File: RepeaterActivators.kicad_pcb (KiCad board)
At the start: 4 copper layers, 60 parts, among them J1 AudioJack1_Grounded, J2 AudioJack2_Grounded, J3 Conn_01x06_Female, J4 8PRJ45_LED_Shielded_Radio1, J5 8PRJ45_LED_Shielded_Radio2, J6 Conn_01x02_Female, J7 Conn_01x02_Female, J8 Conn_01x02_Female, Q1 2N7000, Q2 2N7000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

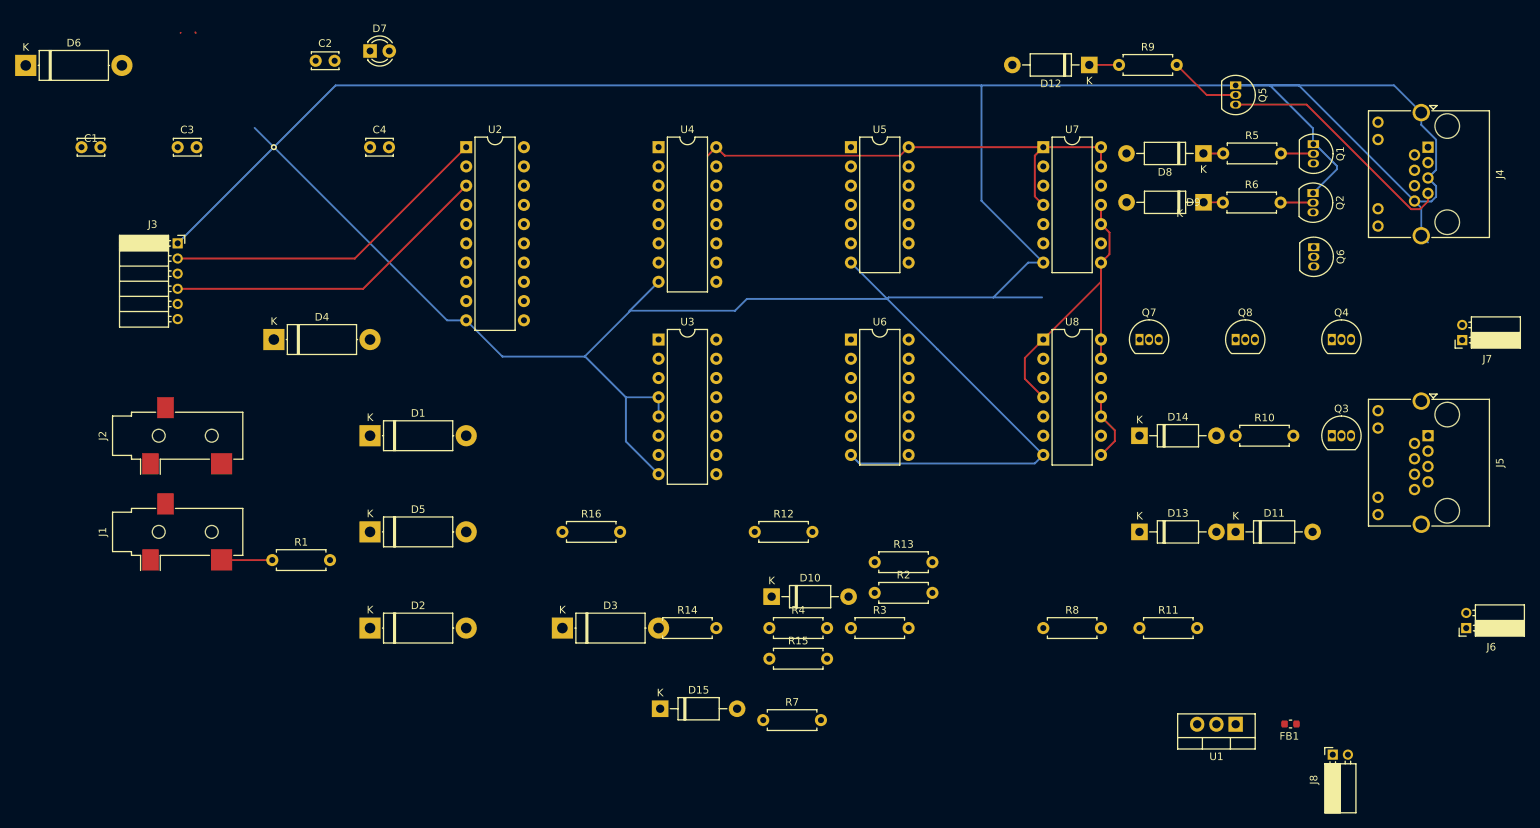
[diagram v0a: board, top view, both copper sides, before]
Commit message: DBD: positioning components on the board
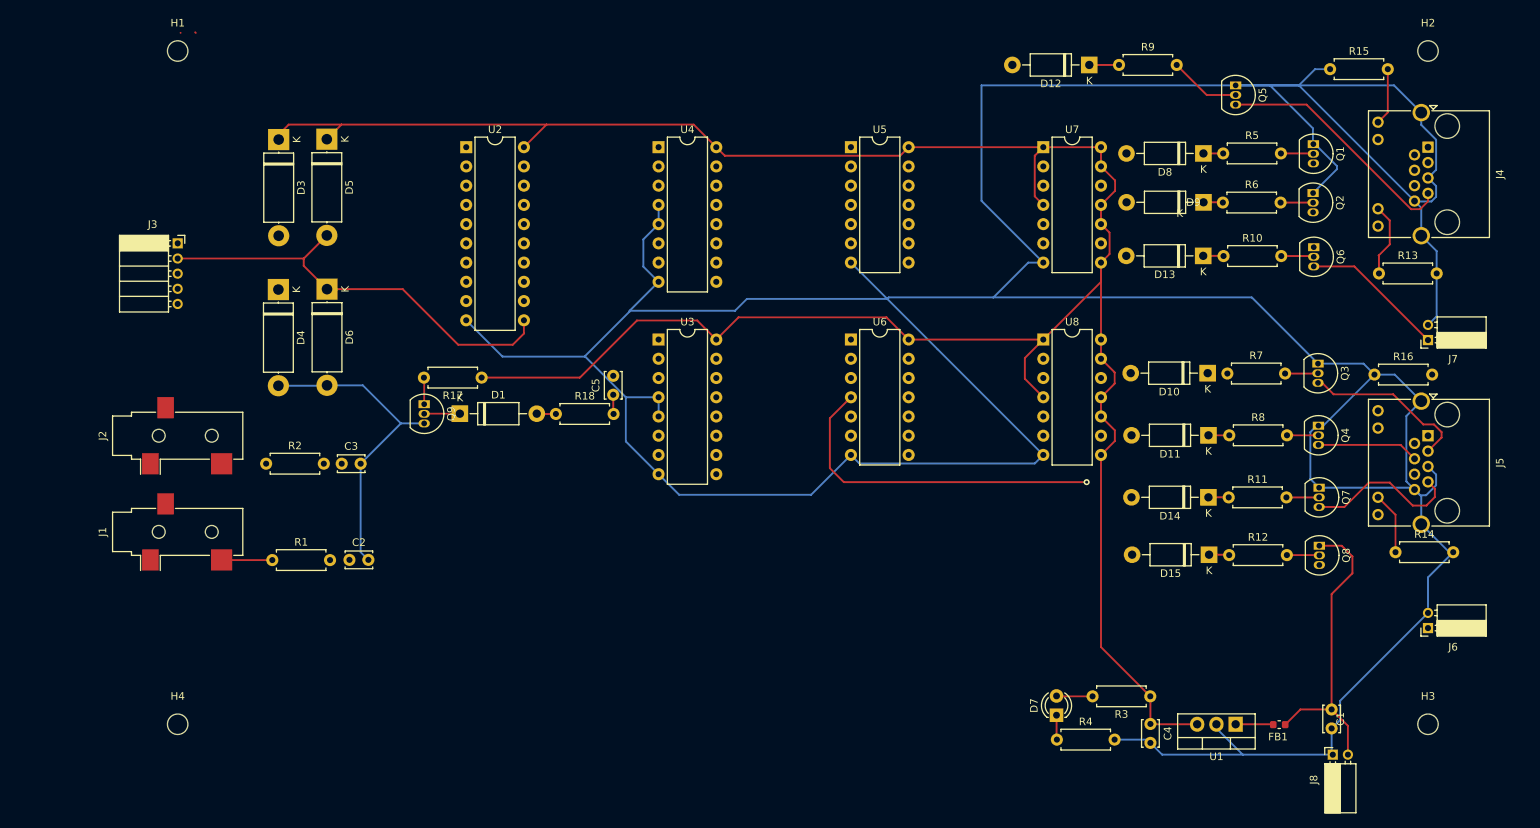
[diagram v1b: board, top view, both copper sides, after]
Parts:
- removed D2: D_Schottky, Diode_THT:D_5W_P12.70mm_Horizontal
- added C5: 100m, Capacitor_THT:C_Disc_D3.4mm_W2.1mm_P2.50mm, F.Cu at (133.7, 70.8)
- added H1: MountingHole, MountingHole:MountingHole_2.7mm_M2.5, F.Cu at (76.2, 25.4)
- added H2: MountingHole, MountingHole:MountingHole_2.7mm_M2.5, F.Cu at (241.3, 25.4)
- added H3: MountingHole, MountingHole:MountingHole_2.7mm_M2.5, F.Cu at (241.3, 114.3)
- added H4: MountingHole, MountingHole:MountingHole_2.7mm_M2.5, F.Cu at (76.2, 114.3)
- added Q9: 2N7000, Package_TO_SOT_THT:TO-92_Inline, F.Cu at (108.7, 72.0)
- added R17: 500, Resistor_THT:R_Axial_DIN0207_L6.3mm_D2.5mm_P7.62mm_Horizontal, F.Cu at (116.3, 68.5)
- added R18: 500, Resistor_THT:R_Axial_DIN0207_L6.3mm_D2.5mm_P7.62mm_Horizontal, F.Cu at (126.1, 73.3)
- D1: value D_Schottky -> 1N4001; footprint Diode_THT:D_5W_P12.70mm_Horizontal -> Diode_THT:D_DO-41_SOD81_P10.16mm_Horizontal
- J3: value Conn_01x06_Female -> Conn_01x05_Female; footprint Connector_PinSocket_2.00mm:PinSocket_1x06_P2.00mm_Horizontal -> Connector_PinSocket_2.00mm:PinSocket_1x05_P2.00mm_Horizontal
- moved C1 181.0 mm to (228.6, 112.3), turned to -90 degrees
- moved C4 128.1 mm to (204.6, 114.3), turned to -90 degrees
- moved D7 126.1 mm to (192.2, 113.1), turned to 90 degrees
- moved R16 109.2 mm to (234.2, 68.1)
- moved R15 107.4 mm to (228.4, 27.8)
- moved R14 97.8 mm to (237.0, 91.6)
- moved R2 82.2 mm to (87.9, 79.9)
- moved R13 76.7 mm to (234.8, 54.8)
- moved R7 76.5 mm to (214.8, 68.0)
- moved D15 75.3 mm to (212.4, 91.9), turned to 180 degrees
- moved D3 74.6 mm to (89.5, 37.1), turned to -90 degrees
- moved C2 66.1 mm to (98.9, 92.6)
- moved D10 64.7 mm to (212.2, 67.9), turned to 180 degrees
- moved R12 62.7 mm to (215.0, 92.0)
- moved D5 52.2 mm to (95.9, 37.0), turned to -90 degrees
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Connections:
- D1 pad 1: /|CLR -> Net-(D1-Pad1)
- D1 pad 2: GND -> Net-(D1-Pad2)
- J3 pad 2: /|CLR -> /Clock Pulse
- J3 pad 3: /Clock Pulse -> /Data Input
- J3 pad 4: /Data Input -> SPI_RPi_Radio2
- J3 pad 5: SPI_RPi_Radio2 -> SPI_RPi_Radio1
- U2 pad 1: /|CLR -> Net-(U2-Pad1)
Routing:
- net +5V: track 117.8 -> 321.7 mm
- net GND: track 495.0 -> 627.9 mm, vias 1 -> 0
- net +12V: track 0.02 -> 87.6 mm
- net Net-(D11-Pad2): track 0.00 -> 55.4 mm, vias 0 -> 1
- net Net-(D10-Pad2): track 0.00 -> 52.0 mm
- net /|CLR: track 44.2 -> 0.00 mm
- net Net-(U2-Pad1): track 0.00 -> 36.3 mm
- net Net-(D14-Pad2): track 0.00 -> 32.9 mm
- net Net-(D15-Pad2): track 0.00 -> 23.8 mm
- net /Radio2 Frequency Down: track 0.00 -> 22.3 mm
- net Net-(J5-Pad7): track 0.00 -> 20.7 mm
- net /Radio1 Fan: track 0.55 -> 19.1 mm
- net /Radio2 Fan: track 0.00 -> 17.8 mm
- net /Radio2 Frequency Up: track 0.00 -> 13.4 mm
- net Net-(J4-Pad11): track 0.00 -> 9.81 mm
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
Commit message: DBD: Routing complete sans minor errors
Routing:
- net SPI_RPi_Radio1: track 0.00 -> 228.5 mm, vias 0 -> 1
- net Audio_RPi_Radio1: track 0.00 -> 211.8 mm
- net SPI_RPi_Radio2: track 0.00 -> 195.4 mm, vias 0 -> 1
- net Audio_RPi_Radio2: track 0.00 -> 159.4 mm, vias 0 -> 2
- net Net-(U3-Pad10): track 0.00 -> 93.4 mm, vias 0 -> 3
- net Net-(U3-Pad11): track 0.00 -> 77.4 mm, vias 0 -> 3
- net GND: track 627.9 -> 700.2 mm
- net Net-(D8-Pad2): track 0.09 -> 71.2 mm
- net Net-(U3-Pad12): track 0.00 -> 67.9 mm, vias 0 -> 1
- net Net-(U4-Pad14): track 0.00 -> 66.4 mm, vias 0 -> 2
- net Net-(U2-Pad2): track 0.00 -> 56.1 mm
- net Net-(U5-Pad2): track 0.00 -> 52.5 mm
- net Net-(U4-Pad6): track 0.00 -> 52.3 mm
- net Net-(U2-Pad13): track 0.00 -> 49.0 mm, vias 0 -> 1
- net Net-(U2-Pad6): track 0.00 -> 48.9 mm, vias 0 -> 1
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
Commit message: DBD: fixed some silkscreen overlaps
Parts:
- moved C5 0.31 mm to (133.7, 70.5)
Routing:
- net Net-(U3-Pad13): vias 3 -> 2

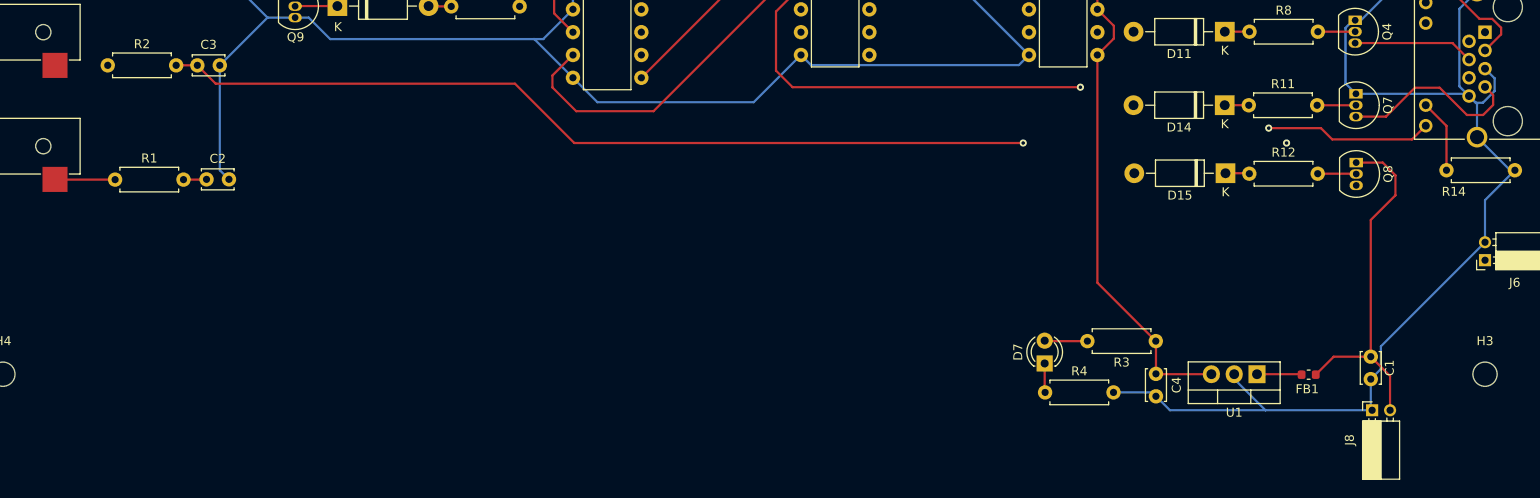
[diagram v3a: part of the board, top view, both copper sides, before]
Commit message: DBD: shrank board a bit
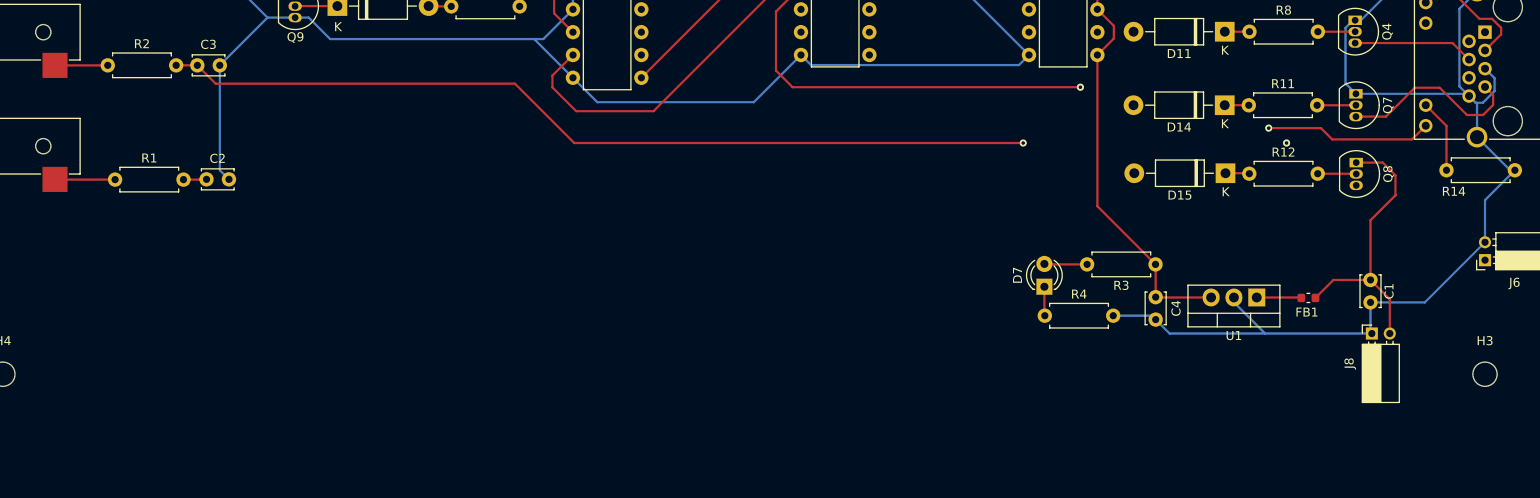
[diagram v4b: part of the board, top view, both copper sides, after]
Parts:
- moved C4 8.55 mm to (204.6, 105.7)
- moved D7 8.55 mm to (192.2, 104.6)
- moved R3 8.55 mm to (204.6, 102.1)
- moved R4 8.55 mm to (192.3, 107.8)
- moved U1 8.55 mm to (215.9, 105.8)
- moved C1 8.55 mm to (228.5, 103.8)
- moved FB1 8.55 mm to (221.6, 105.8)
- moved J8 8.55 mm to (228.7, 109.8)
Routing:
- net +5V: track 321.7 -> 313.2 mm
- net +12V: track 87.5 -> 79.0 mm
- net Net-(J2-PadT): track 0.00 -> 5.88 mm
- net GND: track 700.4 -> 695.4 mm
- net SPI_RPi_Radio1: track 228.5 -> 225.9 mm
- net Audio_RPi_Radio1: track 211.8 -> 210.2 mm

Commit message: DBD: Labelling
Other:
- board text added: "SN74LS04"
- board text added: "SN74LS107"
- board text added: "SN74LS138"
- board text added: "SN74LS273"
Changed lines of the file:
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@@
     )
+  )
+  (gr_text "SN74LS273" (at 118.453934 33.935757) (layer "F.Cu")
+    (effects (font (size 1.5 1.5) (thickness 0.3)))
+  )
+  (gr_text "SN74LS04" (at 169.198587 34.227953) (layer "F.Cu")
+    (effects (font (size 1.5 1.5) (thickness 0.3)))
+  )
+  (gr_text "SN74LS107" (at 194.487894 34.04645) (layer "F.Cu")
+    (effects (font (size 1.5 1.5) (thickness 0.3)))
+  )
+  (gr_text "SN74LS138" (at 143.773491 34.026508) (layer "F.Cu")
+    (effects (font (size 1.5 1.5) (thickness 0.3)))
   )
   (segment (start 231.324247 92.143716) (end 229.90761 90.727079) (width 0.25) (layer "F.Cu") (net 1))
